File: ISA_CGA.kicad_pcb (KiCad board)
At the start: 2 copper layers, 122 parts, among them J1 VIDEO JACK, J2 RGBI Output, P1 1X4 BERG, P2 1X6 BERG, P5 Bus_ISA_8bit, Q1 2N3904, U1 74S112, U10 74153, U101 74S174, U11 74LS74, U12 74LS393, U13 74LS08, U14 74LS32, U15 74LS00, U16 74LS04, U17 74LS138, U18 74LS138, U19 74LS138, U2 74LS74, U20 74LS04, U21 74LS174, U22 74LS51, U23 74LS32, U24 74LS244, U25 74LS00, U26 74S04, U27 74LS51, U28 74LS10, U29 74S04, U3 74S86, U30 74LS32, U31 74S08, U32 74LS166, U33 27C256, U34 74LS273, U35 74LS273, U36 74LS244, U37 74LS374, U38 MC6845, U39 74LS174, U4 74S174, U40 74LS174, U41 74LS08, U42 74LS86, U43 74S74, U44 74S74, U45 74LS151, U46 74LS00, U47 74LS51, U48 74LS51, U49 74LS02, U5 74S174, U50 2118, U51 2118, U52 2118, U53 2118, U54 2118, U55 2118, U56 2118, U57 2118, U58 74LS374, U59 74LS374, U6 74LS04, U60 74LS374, U61 74LS374, U62 74LS125, U63 74LS175, U64 74LS164, U65 74LS02, U66 74LS245, U67 74LS244, U68 74LS86, U7 74LS166, U8 74LS166, U9 74153

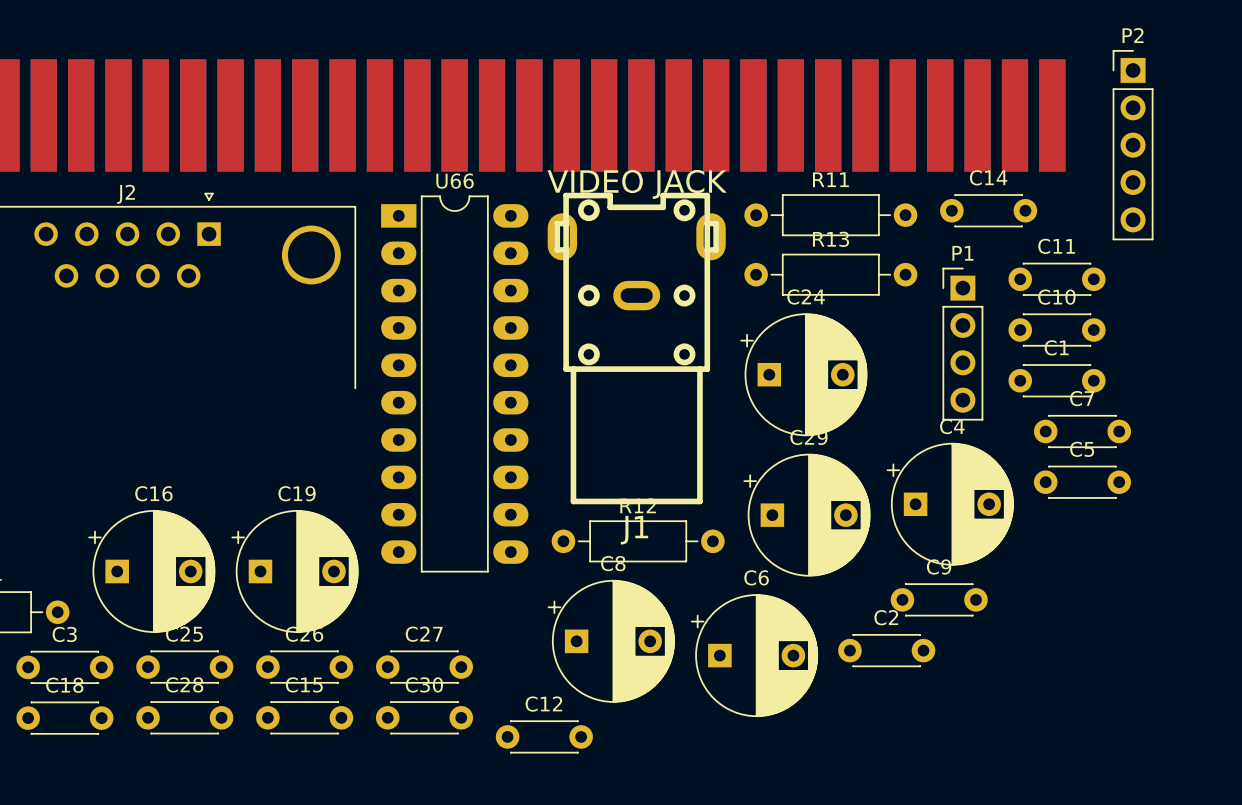
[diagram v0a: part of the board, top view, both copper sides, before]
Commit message: Fixed some footprints
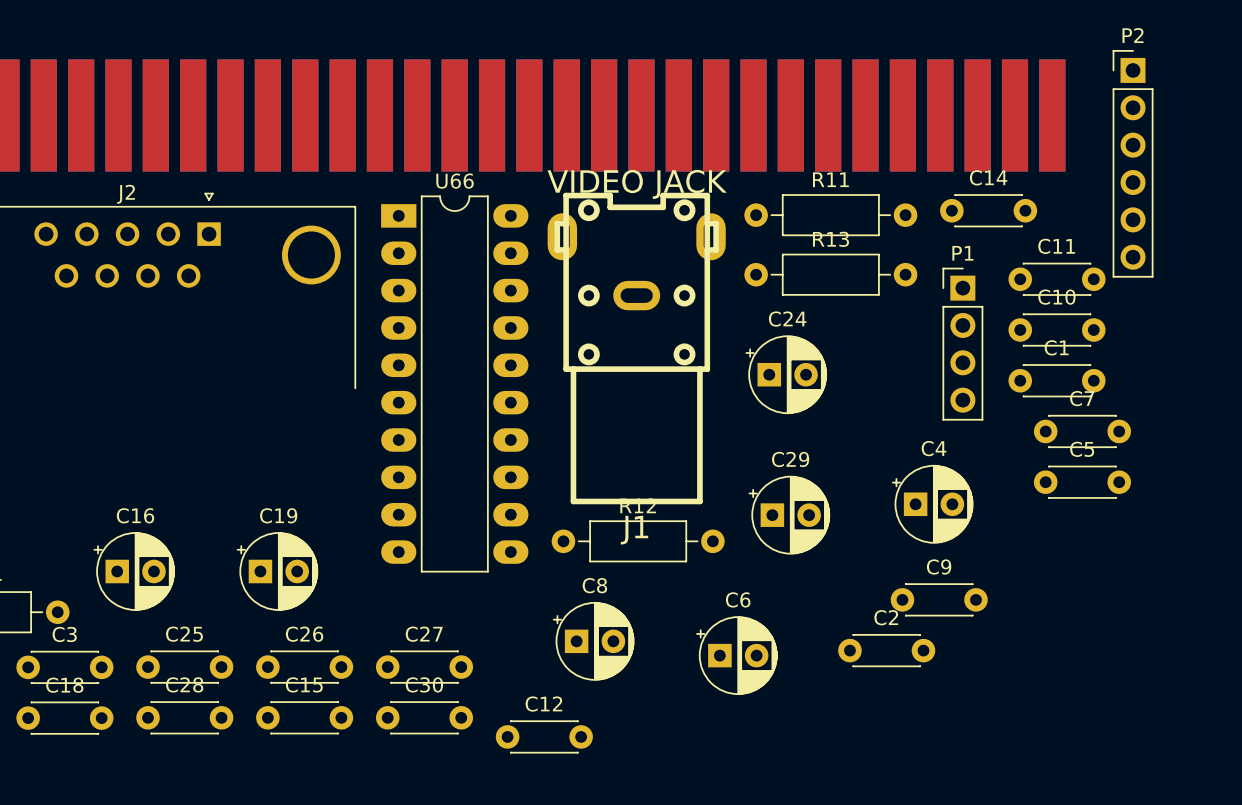
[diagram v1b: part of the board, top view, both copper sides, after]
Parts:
- C16, C19, C24, C29, C4, C6, C8: footprint Capacitor_THT:CP_Radial_D8.0mm_P5.00mm -> Capacitor_THT:CP_Radial_D5.0mm_P2.50mm
- P2: footprint Connector_PinHeader_2.54mm:PinHeader_1x05_P2.54mm_Vertical -> Connector_PinHeader_2.54mm:PinHeader_1x06_P2.54mm_Vertical

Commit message: Add filter caps for every IC
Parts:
- removed the C1 at (202.4, 135.9)
- removed the C25 at (143.1, 155.4)
- removed the C26 at (151.3, 155.4)
- removed the C27 at (159.4, 155.4)
- added C29: 100nF, Capacitor_THT:C_Disc_D4.3mm_W1.9mm_P5.00mm, F.Cu at (319.2, -163.6)
- added C30: 100nF, Capacitor_THT:C_Disc_D4.3mm_W1.9mm_P5.00mm, F.Cu at (319.2, -160.1)
- added C34: 100nF, Capacitor_THT:C_Disc_D4.3mm_W1.9mm_P5.00mm, F.Cu at (319.2, -156.7)
- added C35: 100nF, Capacitor_THT:C_Disc_D4.3mm_W1.9mm_P5.00mm, F.Cu at (327.4, -167.0)
- added C36: 100nF, Capacitor_THT:C_Disc_D4.3mm_W1.9mm_P5.00mm, F.Cu at (335.5, -173.9)
- added C37: 100nF, Capacitor_THT:C_Disc_D4.3mm_W1.9mm_P5.00mm, F.Cu at (335.5, -184.3)
- added C38: 100nF, Capacitor_THT:C_Disc_D4.3mm_W1.9mm_P5.00mm, F.Cu at (335.5, -177.4)
- added C39: 100nF, Capacitor_THT:C_Disc_D4.3mm_W1.9mm_P5.00mm, F.Cu at (343.7, -177.4)
- added C40: 100nF, Capacitor_THT:C_Disc_D4.3mm_W1.9mm_P5.00mm, F.Cu at (335.5, -170.5)
- added C41: 100nF, Capacitor_THT:C_Disc_D4.3mm_W1.9mm_P5.00mm, F.Cu at (327.4, -163.6)
- added C42: 100nF, Capacitor_THT:C_Disc_D4.3mm_W1.9mm_P5.00mm, F.Cu at (327.4, -160.1)
- added C43: 100nF, Capacitor_THT:C_Disc_D4.3mm_W1.9mm_P5.00mm, F.Cu at (360.0, -187.7)
- added C44: 100nF, Capacitor_THT:C_Disc_D4.3mm_W1.9mm_P5.00mm, F.Cu at (327.4, -156.7)
- added C45: 100nF, Capacitor_THT:C_Disc_D4.3mm_W1.9mm_P5.00mm, F.Cu at (335.5, -167.0)
- added C46: 100nF, Capacitor_THT:C_Disc_D4.3mm_W1.9mm_P5.00mm, F.Cu at (351.8, -156.7)
- added C47: 100nF, Capacitor_THT:C_Disc_D4.3mm_W1.9mm_P5.00mm, F.Cu at (351.8, -180.8)
- added C48: 100nF, Capacitor_THT:C_Disc_D4.3mm_W1.9mm_P5.00mm, F.Cu at (360.0, -184.3)
- added C49: 100nF, Capacitor_THT:C_Disc_D4.3mm_W1.9mm_P5.00mm, F.Cu at (351.8, -177.4)
- added C51: 100nF, Capacitor_THT:C_Disc_D4.3mm_W1.9mm_P5.00mm, F.Cu at (343.7, -170.5)
- added C52: 100nF, Capacitor_THT:C_Disc_D4.3mm_W1.9mm_P5.00mm, F.Cu at (335.5, -163.6)
- added C53: 100nF, Capacitor_THT:C_Disc_D4.3mm_W1.9mm_P5.00mm, F.Cu at (335.5, -160.1)
- added C54: 100nF, Capacitor_THT:C_Disc_D4.3mm_W1.9mm_P5.00mm, F.Cu at (368.1, -187.7)
- added C55: 100nF, Capacitor_THT:C_Disc_D4.3mm_W1.9mm_P5.00mm, F.Cu at (360.0, -167.0)
- added C56: 100nF, Capacitor_THT:C_Disc_D4.3mm_W1.9mm_P5.00mm, F.Cu at (343.7, -173.9)
- added C57: 100nF, Capacitor_THT:C_Disc_D4.3mm_W1.9mm_P5.00mm, F.Cu at (351.8, -173.9)
- added C58: 100nF, Capacitor_THT:C_Disc_D4.3mm_W1.9mm_P5.00mm, F.Cu at (360.0, -180.8)
- added C59: 100nF, Capacitor_THT:C_Disc_D4.3mm_W1.9mm_P5.00mm, F.Cu at (368.1, -184.3)
- added C60: 100nF, Capacitor_THT:C_Disc_D4.3mm_W1.9mm_P5.00mm, F.Cu at (360.0, -177.4)
- added C61: 100nF, Capacitor_THT:C_Disc_D4.3mm_W1.9mm_P5.00mm, F.Cu at (351.8, -170.5)
- added C62: 100nF, Capacitor_THT:C_Disc_D4.3mm_W1.9mm_P5.00mm, F.Cu at (343.7, -163.6)
- added C63: 100nF, Capacitor_THT:C_Disc_D4.3mm_W1.9mm_P5.00mm, F.Cu at (343.7, -160.1)
- added C64: 100nF, Capacitor_THT:C_Disc_D4.3mm_W1.9mm_P5.00mm, F.Cu at (335.5, -156.7)
- added C65: 100nF, Capacitor_THT:C_Disc_D4.3mm_W1.9mm_P5.00mm, F.Cu at (351.8, -167.0)
- added C66: 100nF, Capacitor_THT:C_Disc_D4.3mm_W1.9mm_P5.00mm, F.Cu at (351.8, -163.6)
- added C67: 100nF, Capacitor_THT:C_Disc_D4.3mm_W1.9mm_P5.00mm, F.Cu at (360.0, -173.9)
- added C68: 100nF, Capacitor_THT:C_Disc_D4.3mm_W1.9mm_P5.00mm, F.Cu at (368.1, -180.8)
- added C69: 100nF, Capacitor_THT:C_Disc_D4.3mm_W1.9mm_P5.00mm, F.Cu at (368.1, -177.4)
- added C70: 100nF, Capacitor_THT:C_Disc_D4.3mm_W1.9mm_P5.00mm, F.Cu at (360.0, -170.5)
- added C71: 100nF, Capacitor_THT:C_Disc_D4.3mm_W1.9mm_P5.00mm, F.Cu at (351.8, -160.1)
- added C72: 100nF, Capacitor_THT:C_Disc_D4.3mm_W1.9mm_P5.00mm, F.Cu at (343.7, -167.0)
- added C73: 100nF, Capacitor_THT:C_Disc_D4.3mm_W1.9mm_P5.00mm, F.Cu at (343.7, -156.7)
- added C74: 100nF, Capacitor_THT:C_Disc_D4.3mm_W1.9mm_P5.00mm, F.Cu at (368.1, -173.9)
- added C75: 100nF, Capacitor_THT:C_Disc_D4.3mm_W1.9mm_P5.00mm, F.Cu at (360.0, -163.6)
- added C76: 100nF, Capacitor_THT:C_Disc_D4.3mm_W1.9mm_P5.00mm, F.Cu at (368.1, -170.5)
- added C77: 100nF, Capacitor_THT:C_Disc_D4.3mm_W1.9mm_P5.00mm, F.Cu at (360.0, -160.1)
- added C78: 100nF, Capacitor_THT:C_Disc_D4.3mm_W1.9mm_P5.00mm, F.Cu at (360.0, -156.7)
- added C79: 100nF, Capacitor_THT:C_Disc_D4.3mm_W1.9mm_P5.00mm, F.Cu at (368.1, -167.0)
- added C8: 100nF, Capacitor_THT:C_Disc_D4.3mm_W1.9mm_P5.00mm, F.Cu at (335.5, -187.7)
- added C80: 100nF, Capacitor_THT:C_Disc_D4.3mm_W1.9mm_P5.00mm, F.Cu at (368.1, -163.6)
- added C9: 100nF, Capacitor_THT:C_Disc_D4.3mm_W1.9mm_P5.00mm, F.Cu at (319.2, -173.9)
- C1: renamed from C30; value 4.7nF -> 100nF
- C10, C11, C12, C13, C14, C15, C17, C18, C2, C28, C3, C33, C5, C7: value 4.7nF -> 100nF
- C16, C19, C4, C6: value 10uF -> 100nF; footprint Capacitor_THT:CP_Radial_D5.0mm_P2.50mm -> Capacitor_THT:C_Disc_D4.3mm_W1.9mm_P5.00mm
- C25: renamed from C9; value 4.7nF -> 100nF
- moved C33 413.2 mm to (351.8, -187.7)
- moved C18 401.6 mm to (343.7, -184.3)
- moved C17 395.7 mm to (335.5, -180.8)
- moved C3 386.4 mm to (319.2, -184.3)
- moved C28 377.3 mm to (327.4, -170.5)
- moved C19 374.0 mm to (327.4, -180.8)
- moved C12 373.4 mm to (327.4, -177.4)
- moved C16 372.7 mm to (327.4, -173.9)
- moved C13 370.2 mm to (319.2, -170.5)
- moved C6 368.7 mm to (327.4, -184.3)
- moved C2 368.3 mm to (343.7, -180.8)
- moved C15 366.6 mm to (319.2, -167.0)
- moved C4 357.3 mm to (327.4, -187.7)
- moved C10 350.2 mm to (351.8, -184.3)
- moved C14 344.5 mm to (343.7, -187.7)
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- renumbered C8 to C24, C24 to C26, C29 to C27
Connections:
- C16 pad 1: VCC -> GND
- C16 pad 2: GND -> VCC
- C19 pad 1: VCC -> GND
- C19 pad 2: GND -> VCC
- C4 pad 1: VCC -> GND
- C4 pad 2: GND -> VCC
- C6 pad 1: VCC -> GND
- C6 pad 2: GND -> VCC

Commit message: Begin laying out ICs
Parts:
- moved C2 466.3 mm to (52.7, 183.5)
- moved C3 434.4 mm to (52.7, 158.8)
- moved C4 421.1 mm to (52.7, 131.4)
- moved U46 351.8 mm to (51.4, 212.1)
- moved U29 287.2 mm to (51.4, 187.3)
- moved U25 284.8 mm to (51.4, 162.6)
- moved C1 276.1 mm to (52.7, 208.3)
- moved U1 260.0 mm to (51.4, 135.3)
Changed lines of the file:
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@@
   )
   (module Capacitor_THT:C_Disc_D4.3mm_W1.9mm_P5.00mm (layer F.Cu)
-    (at 327.362 -187.748)
+    (at 52.705 131.445)
     (descr "C, Disc series, Radial, pin pitch=5.00mm, , diameter*width=4.3*1.9mm^2, Capacitor, http://www.vishay.com/docs/45233/krseries.pdf")
     (tags "C Disc series Radial pin pitch 5.00mm  diameter 4.3mm width 1.9mm Capacitor")
-    (fp_text reference C4 (at 2.5 -2.2) (layer F.SilkS)
+    (fp_text reference C4 (at -2.54 0) (layer F.SilkS)
       (effects (font (size 1 1) (thickness 0.15)))
     )
@@
   )
   (module Capacitor_THT:C_Disc_D4.3mm_W1.9mm_P5.00mm (layer F.Cu)
-    (at 319.212 -184.298)
+    (at 52.705 158.75)
     (descr "C, Disc series, Radial, pin pitch=5.00mm, , diameter*width=4.3*1.9mm^2, Capacitor, http://www.vishay.com/docs/45233/krseries.pdf")
     (tags "C Disc series Radial pin pitch 5.00mm  diameter 4.3mm width 1.9mm Capacitor")
-    (fp_text reference C3 (at 2.5 -2.2) (layer F.SilkS)
+    (fp_text reference C3 (at -2.54 0) (layer F.SilkS)
       (effects (font (size 1 1) (thickness 0.15)))
     )
@@
   )
   (module Capacitor_THT:C_Disc_D4.3mm_W1.9mm_P5.00mm (layer F.Cu)
-    (at 343.662 -180.848)
+    (at 52.705 183.515)
     (descr "C, Disc series, Radial, pin pitch=5.00mm, , diameter*width=4.3*1.9mm^2, Capacitor, http://www.vishay.com/docs/45233/krseries.pdf")
     (tags "C Disc series Radial pin pitch 5.00mm  diameter 4.3mm width 1.9mm Capacitor")
-    (fp_text reference C2 (at 2.5 -2.2) (layer F.SilkS)
+    (fp_text reference C2 (at -2.54 0) (layer F.SilkS)
       (effects (font (size 1 1) (thickness 0.15)))
     )
@@
   )
   (module Package_DIP:DIP-14_W7.62mm_LongPads (layer F.Cu)
-    (at 125.244 -131.882)
+    (at 51.435 212.09)
     (descr "14-lead though-hole mounted DIP package, row spacing 7.62 mm (300 mils), LongPads")
     (tags "THT DIP DIL PDIP 2.54mm 7.62mm 300mil LongPads")
-    (fp_text reference U46 (at 3.81 -2.33) (layer F.SilkS)
+    (fp_text reference U46 (at -2.54 0 90) (layer F.SilkS)
       (effects (font (size 1 1) (thickness 0.15)))
     )
@@
   )
   (module Package_DIP:DIP-14_W7.62mm_LongPads (layer F.Cu)
-    (at 113.644 -93.082)
+    (at 51.435 187.325)
     (descr "14-lead though-hole mounted DIP package, row spacing 7.62 mm (300 mils), LongPads")
     (tags "THT DIP DIL PDIP 2.54mm 7.62mm 300mil LongPads")
-    (fp_text reference U29 (at 3.81 -2.33) (layer F.SilkS)
+    (fp_text reference U29 (at -2.54 0 90) (layer F.SilkS)
       (effects (font (size 1 1) (thickness 0.15)))
     )
@@
   )
   (module Package_DIP:DIP-14_W7.62mm_LongPads (layer F.Cu)
-    (at 125.244 -112.482)
+    (at 51.435 162.56)
     (descr "14-lead though-hole mounted DIP package, row spacing 7.62 mm (300 mils), LongPads")
     (tags "THT DIP DIL PDIP 2.54mm 7.62mm 300mil LongPads")
-    (fp_text reference U25 (at 3.81 -2.33) (layer F.SilkS)
+    (fp_text reference U25 (at -2.54 0 90) (layer F.SilkS)
       (effects (font (size 1 1) (thickness 0.15)))
     )
@@
   )
   (module Package_DIP:DIP-16_W7.62mm_LongPads (layer F.Cu)
-    (at 67.244 -124.282)
+    (at 51.435 135.255)
     (descr "16-lead though-hole mounted DIP package, row spacing 7.62 mm (300 mils), LongPads")
     (tags "THT DIP DIL PDIP 2.54mm 7.62mm 300mil LongPads")
-    (fp_text reference U1 (at 3.81 -2.33) (layer F.SilkS)
+    (fp_text reference U1 (at -2.54 -0.635 90) (layer F.SilkS)
       (effects (font (size 1 1) (thickness 0.15)))
     )
@@
   )
   (module Capacitor_THT:C_Disc_D4.3mm_W1.9mm_P5.00mm (layer F.Cu)
-    (at 198.544 -26.102)
+    (at 52.705 208.28)
     (descr "C, Disc series, Radial, pin pitch=5.00mm, , diameter*width=4.3*1.9mm^2, Capacitor, http://www.vishay.com/docs/45233/krseries.pdf")
     (tags "C Disc series Radial pin pitch 5.00mm  diameter 4.3mm width 1.9mm Capacitor")
-    (fp_text reference C1 (at 2.5 -2.2) (layer F.SilkS)
+    (fp_text reference C1 (at -2.54 0) (layer F.SilkS)
       (effects (font (size 1 1) (thickness 0.15)))
     )

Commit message: Laying out more components
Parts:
- U30: footprint Package_DIP:DIP-14_W10.16mm_LongPads -> Package_DIP:DIP-14_W7.62mm_LongPads
- moved C5 463.9 mm to (66.7, 208.3)
- moved C10 457.0 mm to (80.6, 183.5)
- moved C6 450.8 mm to (66.7, 183.5)
- moved C9 450.6 mm to (80.6, 208.3)
- moved C14 445.0 mm to (94.6, 181.0)
- moved C13 440.4 mm to (94.6, 208.3)
- moved C11 420.2 mm to (80.6, 158.1)
- moved C7 419.9 mm to (66.7, 158.1)
- moved C8 416.8 mm to (66.7, 130.8)
- moved C15 395.2 mm to (94.6, 158.1)
- moved C12 394.8 mm to (80.6, 130.8)
- moved C16 383.5 mm to (94.6, 130.8)
- moved U32 381.7 mm to (93.3, 184.8)
- moved U31 351.0 mm to (79.4, 187.3)
- moved U30 329.8 mm to (65.4, 187.3)
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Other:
- net class POWER added: clearance 0.25, trace_width 0.5, via_dia 0.8, via_drill 0.4
- net class POWER_Small added: clearance 0.25, trace_width 0.35, via_dia 0.8, via_drill 0.4

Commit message: Additional layout
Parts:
- moved C18 449.0 mm to (125.7, 208.3)
- moved C17 448.9 mm to (111.8, 208.3)
- moved C19 432.0 mm to (139.7, 208.3)
- moved C33 425.7 mm to (195.6, 208.3)
- moved C28 416.7 mm to (153.7, 208.3)
- moved C29 401.6 mm to (167.6, 208.3)
- moved C30 393.3 mm to (181.6, 208.3)
- moved C35 390.8 mm to (114.3, 160.5)
- moved C34 381.1 mm to (209.6, 208.3)
- moved C37 380.9 mm to (121.9, 131.1)
- moved C36 380.1 mm to (108.7, 131.1)
- moved C38 367.6 mm to (135.6, 131.1)
- moved C39 364.6 mm to (149.4, 131.1)
- moved C40 347.1 mm to (163.6, 131.1)
- moved U33 331.2 mm to (109.2, 164.6)
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
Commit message: Reorganize space between ICs
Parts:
- U14: value 74LS32 -> 74S32
- moved C43 353.6 mm to (206.4, 130.8)
- moved C47 328.4 mm to (248.3, 130.8)
- moved C45 319.3 mm to (220.3, 130.8)
- moved U14 313.5 mm to (219.1, 134.6)
- moved C46 310.6 mm to (234.3, 130.8)
- moved U16 306.4 mm to (247.0, 134.6)
- moved U13 294.9 mm to (205.1, 134.6)
- moved U15 289.2 mm to (233.0, 134.6)
- moved U33 1.28 mm to (108.0, 164.5)
- moved C35 1.27 mm to (113.0, 160.5)
- moved C40 0.92 mm to (164.5, 130.8)
- moved U8 0.89 mm to (149.2, 134.6)
- moved C37 0.68 mm to (122.6, 130.8)
- moved C41 0.68 mm to (178.4, 130.8)
- moved C30 0.64 mm to (181.0, 208.3)
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
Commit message: More layout
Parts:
- moved U24 408.3 mm to (358.8, 134.6)
- moved U68 400.7 mm to (358.8, 165.7)
- moved U44 384.3 mm to (330.8, 165.7)
- moved C59 348.1 mm to (332.1, 161.9)
- moved U23 341.4 mm to (344.8, 134.6)
- moved C58 340.5 mm to (346.1, 159.4)
- moved U22 339.1 mm to (330.8, 134.6)
- moved C57 336.0 mm to (360.0, 161.9)
- moved U20 333.7 mm to (302.9, 134.6)
- moved C48 329.9 mm to (262.3, 130.8)
- moved C54 320.6 mm to (332.1, 130.8)
- moved C49 317.3 mm to (276.2, 130.8)
- moved C51 306.0 mm to (290.2, 130.8)
- moved C56 305.2 mm to (360.0, 130.8)
- moved C55 298.2 mm to (346.1, 130.8)
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
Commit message: Reorganize layout a bit
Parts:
- moved U43 358.7 mm to (316.9, 165.7)
- moved C63 345.3 mm to (360.0, 184.8)
- moved C60 341.9 mm to (318.1, 161.9)
- moved C61 335.8 mm to (304.2, 161.9)
- moved C62 329.9 mm to (290.2, 161.9)
- moved U42 324.0 mm to (302.9, 165.7)
- moved U41 319.2 mm to (288.9, 165.7)
- moved U67 98.3 mm to (358.8, 188.6)
- moved U33 0.90 mm to (108.6, 168.3)
- moved C35 0.90 mm to (113.7, 164.3)
- moved C11 0.64 mm to (80.6, 161.9)
- moved C15 0.64 mm to (94.6, 161.9)
- moved C3 0.64 mm to (52.7, 161.9)
- moved C7 0.64 mm to (66.7, 161.9)
- moved U25 0.64 mm to (51.4, 165.7)
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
